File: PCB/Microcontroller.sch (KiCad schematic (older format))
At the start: 25 parts, among them IC1 Atmega32U4, J1 TC2030_IDC_Atmel, J2 2x3_254, Q1 16MHz_KX_7

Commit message: Audio Switch eindesignt
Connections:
- net Input_Select: now reaches IC1.28 (PB4_(PCINT4/ADC11))
- net Output_Select: now reaches IC1.29 (PB5_(PCINT5/OC1A/~OC4B~/ADC12))
- no-connect marks 12 -> 10
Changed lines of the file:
@@
 NoConn ~ 7300 2000
 NoConn ~ 7300 2300
-NoConn ~ 7300 3800
-NoConn ~ 7300 3700
 NoConn ~ 7300 3000
 NoConn ~ 7300 2900
@@
 Text HLabel 7450 2100 2    50   Input ~ 0
 SW1
+Text HLabel 7500 3700 2    39   Output ~ 0
+Input_Select
+Text HLabel 7500 3800 2    39   Output ~ 0
+Output_Select
+Wire Wire Line
+	7300 3800 7500 3800
+Wire Wire Line
+	7300 3700 7500 3700
 $EndSCHEMATC

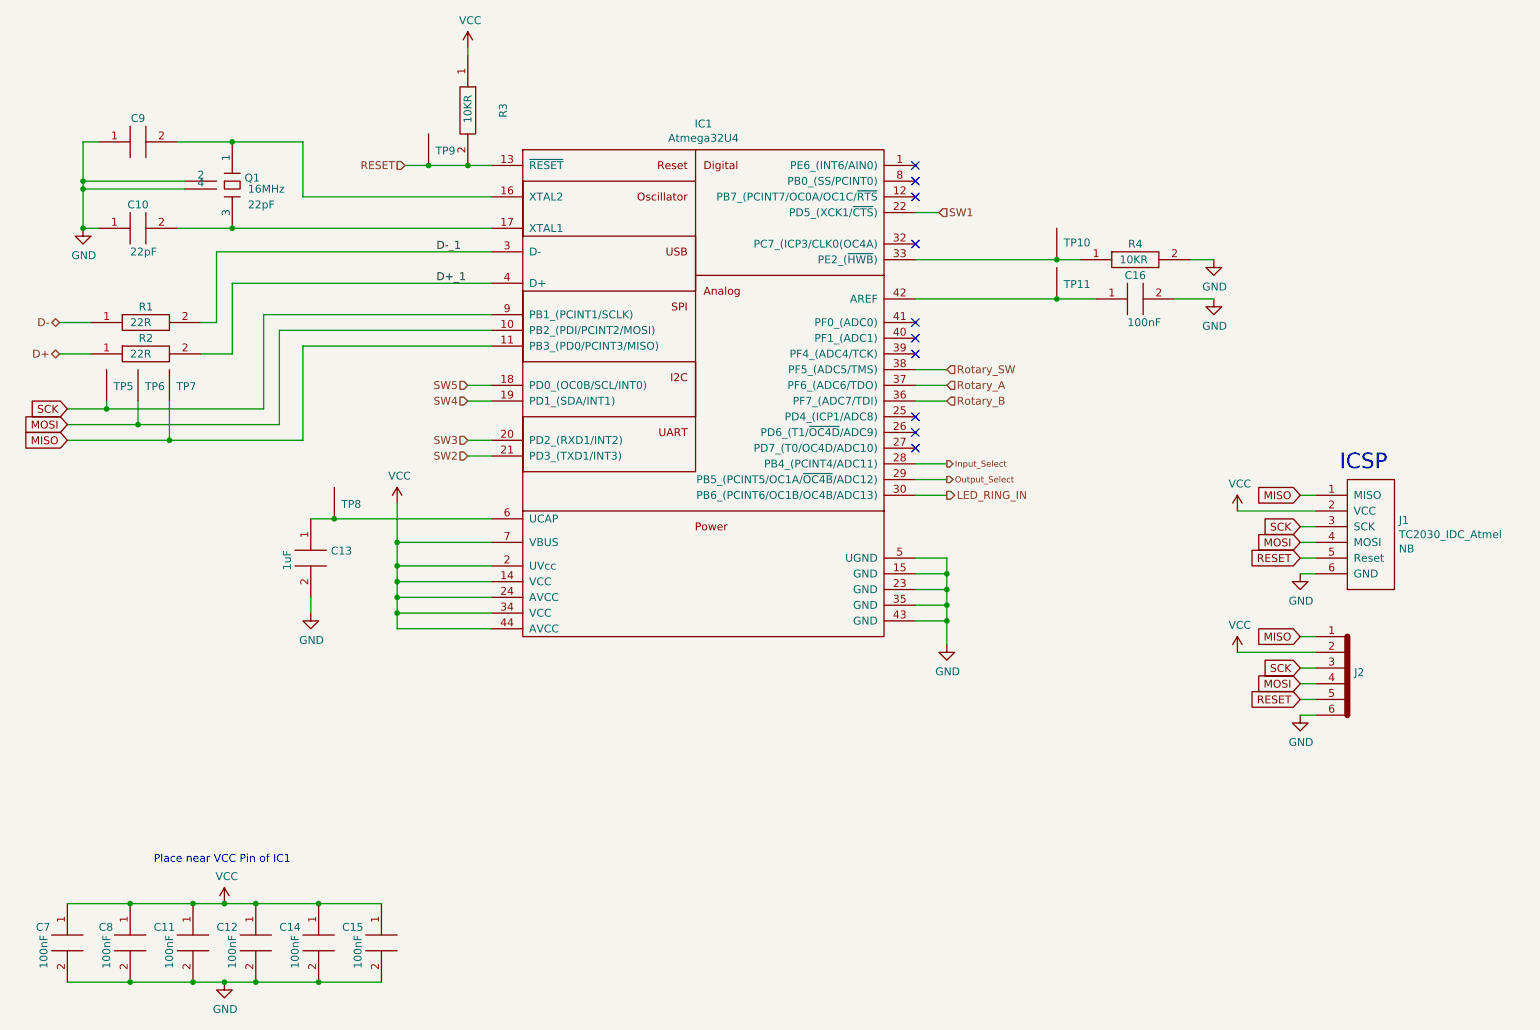
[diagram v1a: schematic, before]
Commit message: Sheet USB
USB Switch und USB Input Stecker hinzugefügt
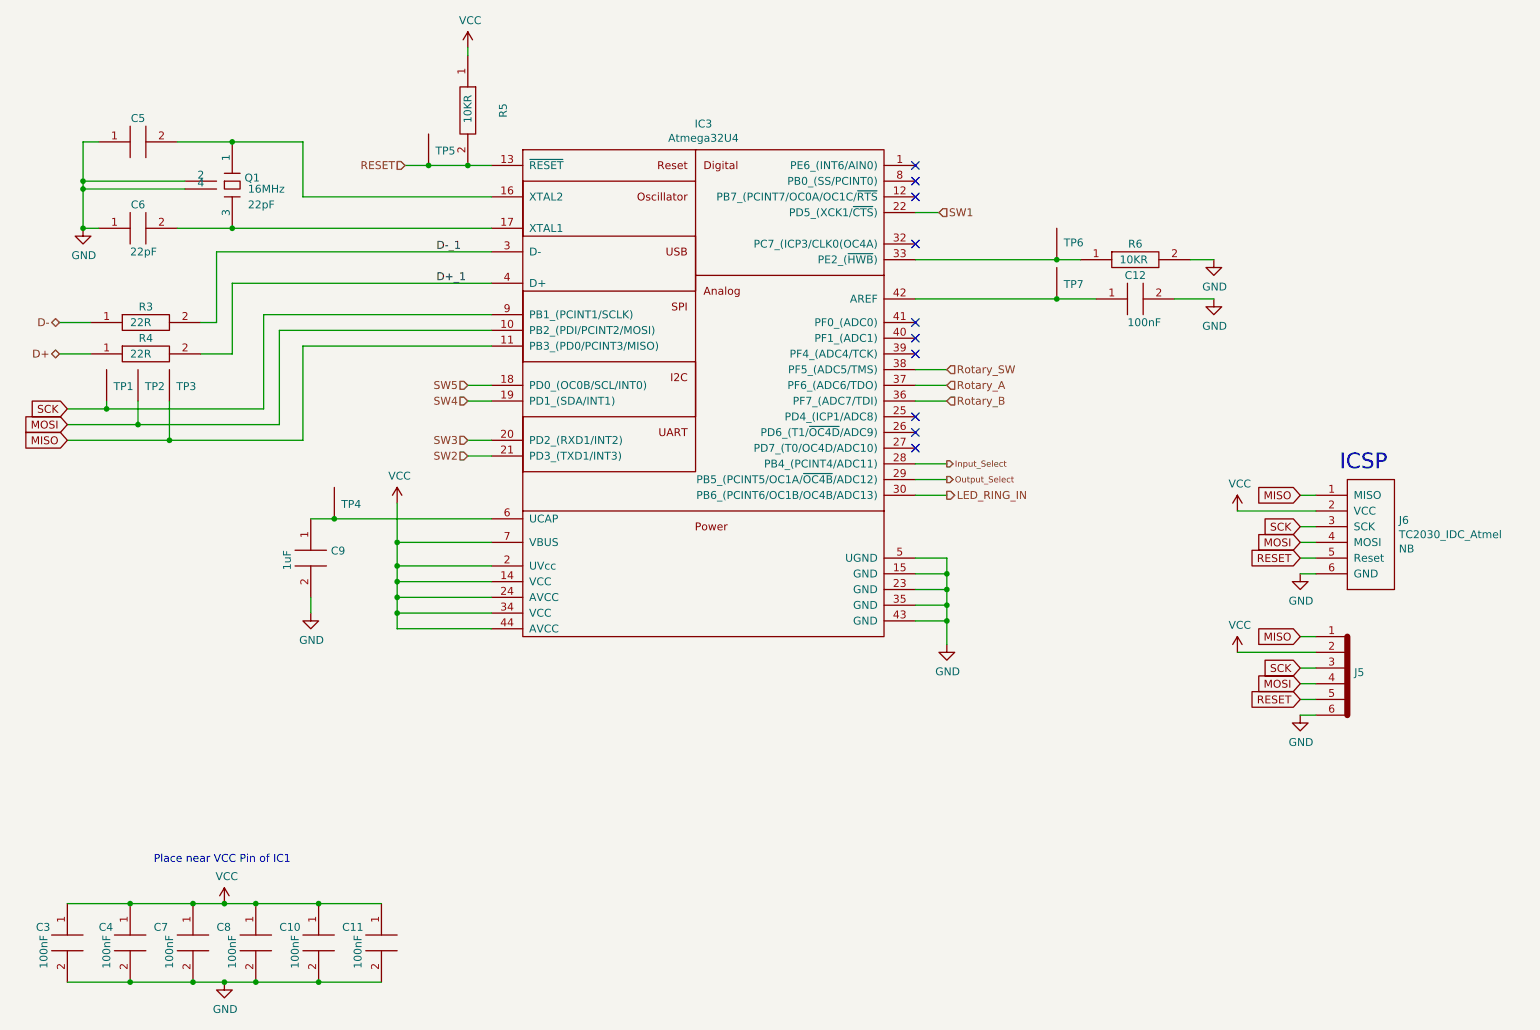
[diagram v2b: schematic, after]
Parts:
- renumbered C14 to C10, C15 to C11, C16 to C12, C7 to C3, C8 to C4, C9 to C5, C10 to C6, C11 to C7, C12 to C8, C13 to C9, IC1 to IC3, J2 to J5, J1 to J6, R1 to R3, R2 to R4, R3 to R5, R4 to R6, TP5 to TP1, TP6 to TP2, TP7 to TP3, TP8 to TP4, TP9 to TP5, TP10 to TP6, TP11 to TP7
